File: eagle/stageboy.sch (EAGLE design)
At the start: 35 parts, among them IC1 MEGA8-P, IC2 7805TV, J1 POWER_JACKPTH, Q1 16MHz, X1 MIDI IN, X2 MIDI OUT, X4 22-23-2021, X6 GBIO

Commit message: Picked a board layout and named it accordingly
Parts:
- renumbered JP2 to GB5V
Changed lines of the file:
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@@
 <part name="C3" library="rcl" deviceset="C-US" device="025-025X050" value="22pF"/>
 <part name="C4" library="rcl" deviceset="C-US" device="025-025X050" value="22pF"/>
-<part name="JP2" library="jumper" deviceset="JP1Q" device="" value="GB5V"/>
+<part name="GB5V" library="jumper" deviceset="JP1Q" device="" value="GB5V"/>
 <part name="SUPPLY20" library="supply2" deviceset="+5V" device=""/>
 <part name="SUPPLY22" library="supply2" deviceset="+5V" device=""/>
@@
 <instance part="C3" gate="G$1" x="33.02" y="68.58" rot="R90"/>
 <instance part="C4" gate="G$1" x="33.02" y="53.34" rot="R90"/>
-<instance part="JP2" gate="A" x="157.48" y="116.84" rot="R180"/>
+<instance part="GB5V" gate="A" x="157.48" y="116.84" rot="R180"/>
 <instance part="SUPPLY20" gate="+5V" x="157.48" y="127"/>
 <instance part="SUPPLY22" gate="+5V" x="101.6" y="124.46" rot="R270"/>
@@
 <segment>
 <pinref part="SUPPLY20" gate="+5V" pin="+5V"/>
-<pinref part="JP2" gate="A" pin="1"/>
+<pinref part="GB5V" gate="A" pin="1"/>
 </segment>
 <segment>
@@
 <segment>
 <pinref part="X6" gate="G$1" pin="4"/>
-<pinref part="JP2" gate="A" pin="2"/>
+<pinref part="GB5V" gate="A" pin="2"/>
 <wire x1="157.48" y1="99.06" x2="157.48" y2="109.22" width="0.1524" layer="91"/>
 </segment>

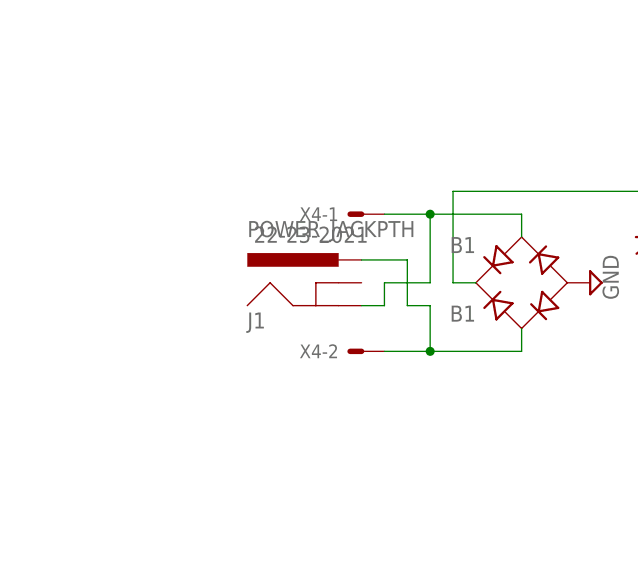
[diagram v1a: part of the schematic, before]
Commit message: Resized the electrolytic capacitors
The 2200uF cap was way too small, with the 22uF being only slightly
so. Both were changed and components shifted around as needed.
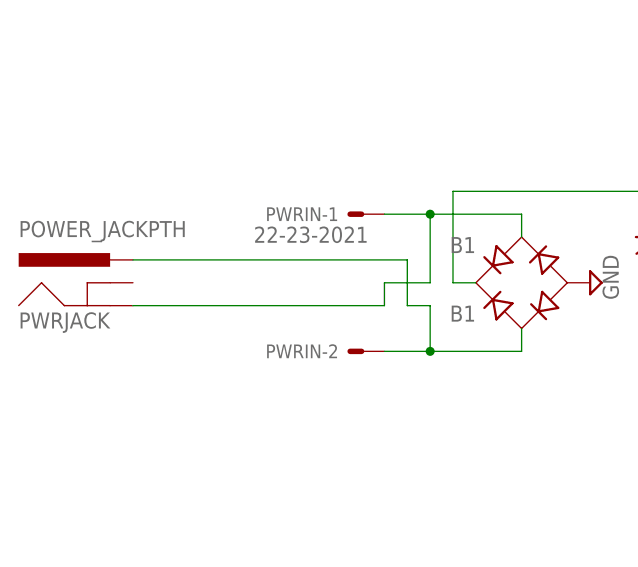
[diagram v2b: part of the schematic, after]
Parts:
- removed J1: POWER_JACKPTH, SparkFun-Connectors:POWER_JACKPTH
- added PWRJACK: POWER_JACKPTH, SparkFun-Connectors:POWER_JACKPTH
- C6: device resistor:CPOL-USE2.5-6 -> resistor:CPOL-USE2.5-7
- C7: device resistor:CPOL-USE3.5-10 -> resistor:CPOL-USE5-13
- renumbered X4 to PWRIN
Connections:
- net N$38: now also PWRJACK.GND; no longer J1.GND
- net N$39: now also PWRJACK.PWR; no longer J1.PWR
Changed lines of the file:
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@@
 <grid distance="0.1" unitdist="inch" unit="inch" style="lines" multiple="1" display="no" altdistance="0.01" altunitdist="inch" altunit="inch"/>
 <layers>
-<layer number="1" name="Top" color="4" fill="1" visible="no" active="no"/>
-<layer number="2" name="Route2" color="1" fill="3" visible="no" active="no"/>
-<layer number="3" name="Route3" color="4" fill="3" visible="no" active="no"/>
-<layer number="14" name="Route14" color="1" fill="6" visible="no" active="no"/>
-<layer number="15" name="Route15" color="4" fill="6" visible="no" active="no"/>
-<layer number="16" name="Bottom" color="1" fill="1" visible="no" active="no"/>
-<layer number="17" name="Pads" color="2" fill="1" visible="no" active="no"/>
-<layer number="18" name="Vias" color="2" fill="1" visible="no" active="no"/>
-<layer number="19" name="Unrouted" color="6" fill="1" visible="no" active="no"/>
-<layer number="20" name="Dimension" color="15" fill="1" visible="no" active="no"/>
-<layer number="21" name="tPlace" color="7" fill="1" visible="no" active="no"/>
-<layer number="22" name="bPlace" color="7" fill="1" visible="no" active="no"/>
-<layer number="23" name="tOrigins" color="15" fill="1" visible="no" active="no"/>
-<layer number="24" name="bOrigins" color="15" fill="1" visible="no" active="no"/>
-<layer number="25" name="tNames" color="7" fill="1" visible="no" active="no"/>
-<layer number="26" name="bNames" color="7" fill="1" visible="no" active="no"/>
-<layer number="27" name="tValues" color="7" fill="1" visible="no" active="no"/>
-<layer number="28" name="bValues" color="7" fill="1" visible="no" active="no"/>
+<layer number="1" name="Top" color="4" fill="1" visible="yes" active="no"/>
+<layer number="2" name="Route2" color="1" fill="3" visible="yes" active="no"/>
+<layer number="3" name="Route3" color="4" fill="3" visible="yes" active="no"/>
+<layer number="14" name="Route14" color="1" fill="6" visible="yes" active="no"/>
+<layer number="15" name="Route15" color="4" fill="6" visible="yes" active="no"/>
+<layer number="16" name="Bottom" color="1" fill="1" visible="yes" active="no"/>
+<layer number="17" name="Pads" color="2" fill="1" visible="yes" active="no"/>
+<layer number="18" name="Vias" color="2" fill="1" visible="yes" active="no"/>
+<layer number="19" name="Unrouted" color="6" fill="1" visible="yes" active="no"/>
+<layer number="20" name="Dimension" color="15" fill="1" visible="yes" active="no"/>
+<layer number="21" name="tPlace" color="7" fill="1" visible="yes" active="no"/>
+<layer number="22" name="bPlace" color="7" fill="1" visible="yes" active="no"/>
+<layer number="23" name="tOrigins" color="15" fill="1" visible="yes" active="no"/>
+<layer number="24" name="bOrigins" color="15" fill="1" visible="yes" active="no"/>
+<layer number="25" name="tNames" color="7" fill="1" visible="yes" active="no"/>
+<layer number="26" name="bNames" color="7" fill="1" visible="yes" active="no"/>
+<layer number="27" name="tValues" color="7" fill="1" visible="yes" active="no"/>
+<layer number="28" name="bValues" color="7" fill="1" visible="yes" active="no"/>
 <layer number="29" name="tStop" color="7" fill="3" visible="no" active="no"/>
 <layer number="30" name="bStop" color="7" fill="6" visible="no" active="no"/>
@@
 <layer number="35" name="tGlue" color="7" fill="4" visible="no" active="no"/>
 <layer number="36" name="bGlue" color="7" fill="5" visible="no" active="no"/>
-<layer number="37" name="tTest" color="7" fill="1" visible="no" active="no"/>
-<layer number="38" name="bTest" color="7" fill="1" visible="no" active="no"/>
+<layer number="37" name="tTest" color="7" fill="1" visible="yes" active="no"/>
+<layer number="38" name="bTest" color="7" fill="1" visible="yes" active="no"/>
 <layer number="39" name="tKeepout" color="4" fill="11" visible="no" active="no"/>
 <layer number="40" name="bKeepout" color="1" fill="11" visible="no" active="no"/>
@@
 <layer number="44" name="Drills" color="7" fill="1" visible="no" active="no"/>
 <layer number="45" name="Holes" color="7" fill="1" visible="no" active="no"/>
-<layer number="46" name="Milling" color="3" fill="1" visible="no" active="no"/>
-<layer number="47" name="Measures" color="7" fill="1" visible="no" active="no"/>
-<layer number="48" name="Document" color="7" fill="1" visible="no" active="no"/>
-<layer number="49" name="Reference" color="7" fill="1" visible="no" active="no"/>
-<layer number="50" name="dxf" color="7" fill="1" visible="no" active="no"/>
-<layer number="51" name="tDocu" color="7" fill="1" visible="no" active="no"/>
-<layer number="52" name="bDocu" color="7" fill="1" visible="no" active="no"/>
-<layer number="53" name="tGND_GNDA" color="7" fill="9" visible="no" active="no"/>
-<layer number="54" name="bGND_GNDA" color="1" fill="9" visible="no" active="no"/>
-<layer number="56" name="wert" color="7" fill="1" visible="no" active="no"/>
+<layer number="46" name="Milling" color="3" fill="1" visible="yes" active="no"/>
+<layer number="47" name="Measures" color="7" fill="1" visible="yes" active="no"/>
+<layer number="48" name="Document" color="7" fill="1" visible="yes" active="no"/>
+<layer number="49" name="Reference" color="7" fill="1" visible="yes" active="no"/>
+<layer number="50" name="dxf" color="7" fill="1" visible="yes" active="no"/>
+<layer number="51" name="tDocu" color="7" fill="1" visible="yes" active="no"/>
+<layer number="52" name="bDocu" color="7" fill="1" visible="yes" active="no"/>
+<layer number="53" name="tGND_GNDA" color="7" fill="9" visible="yes" active="no"/>
+<layer number="54" name="bGND_GNDA" color="1" fill="9" visible="yes" active="no"/>
+<layer number="56" name="wert" color="7" fill="1" visible="yes" active="no"/>
 <layer number="91" name="Nets" color="2" fill="1" visible="yes" active="yes"/>
 <layer number="92" name="Busses" color="1" fill="1" visible="yes" active="yes"/>
@@
 <part name="X2" library="con-hirschmann" deviceset="MAB5SH" device="" value="MIDI OUT"/>
 <part name="MIDI-IN" library="pinhead" deviceset="PINHD-1X2" device="" value="MIDI IN"/>
-<part name="C6" library="resistor" deviceset="CPOL-US" device="E2.5-6" value="22uF"/>
+<part name="C6" library="resistor" deviceset="CPOL-US" device="E2.5-7" value="22uF"/>
 <part name="SUPPLY16" library="supply2" deviceset="GND" device=""/>
-<part name="X4" library="con-molex" deviceset="22-23-2021" device=""/>
+<part name="PWRIN" library="con-molex" deviceset="22-23-2021" device=""/>
 <part name="IC2" library="linear" deviceset="78*" device="TV" technology="05"/>
 <part name="C5" library="rcl" deviceset="C-US" device="025-025X050" value="100nF"/>
@@
 <part name="SUPPLY7" library="supply2" deviceset="GND" device=""/>
 <part name="B1" library="rectifier" deviceset="RB1A" device="" value="B1"/>
-<part name="C7" library="resistor" deviceset="CPOL-US" device="E3.5-10" value="2200uF"/>
+<part name="C7" library="resistor" deviceset="CPOL-US" device="E5-13" value="2200uF"/>
 <part name="C8" library="rcl" deviceset="C-US" device="025-025X050" value="330nF"/>
 <part name="SUPPLY9" library="supply2" deviceset="GND" device=""/>
@@
 <part name="SUPPLY29" library="supply2" deviceset="GND" device=""/>
 <part name="5VDC" library="con-molex" deviceset="22-23-2021" device="" value="DCPWR"/>
-<part name="J1" library="SparkFun-Connectors" deviceset="POWER_JACK" device="PTH"/>
+<part name="PWRJACK" library="SparkFun-Connectors" deviceset="POWER_JACK" device="PTH"/>
 <part name="SUPPLY10" library="supply2" deviceset="GND" device=""/>
 </parts>
@@
 <instance part="C6" gate="G$1" x="86.36" y="119.38"/>
 <instance part="SUPPLY16" gate="GND" x="86.36" y="111.76"/>
-<instance part="X4" gate="-1" x="-10.16" y="121.92" rot="R180"/>
-<instance part="X4" gate="-2" x="-10.16" y="106.68" rot="R180"/>
+<instance part="PWRIN" gate="-1" x="-10.16" y="121.92" rot="R180"/>
+<instance part="PWRIN" gate="-2" x="-10.16" y="106.68" rot="R180"/>
 <instance part="IC2" gate="A1" x="48.26" y="124.46"/>
 <instance part="C5" gate="G$1" x="73.66" y="119.38"/>
@@
 <instance part="5VDC" gate="-1" x="101.6" y="139.7"/>
 <instance part="5VDC" gate="-2" x="101.6" y="137.16"/>
-<instance part="J1" gate="G$1" x="-12.7" y="109.22"/>
+<instance part="PWRJACK" gate="G$1" x="-38.1" y="109.22"/>
 <instance part="SUPPLY10" gate="GND" x="203.2" y="35.56" rot="R90"/>
 </instances>
@@
 <wire x1="7.62" y1="121.92" x2="-2.54" y2="121.92" width="0.1524" layer="91"/>
 <wire x1="-2.54" y1="121.92" x2="-2.54" y2="114.3" width="0.1524" layer="91"/>
-<pinref part="X4" gate="-1" pin="S"/>
+<pinref part="PWRIN" gate="-1" pin="S"/>
 <wire x1="-7.62" y1="121.92" x2="-2.54" y2="121.92" width="0.1524" layer="91"/>
 <junction x="-2.54" y="121.92"/>
 <wire x1="-2.54" y1="114.3" x2="-7.62" y2="114.3" width="0.1524" layer="91"/>
 <wire x1="-7.62" y1="114.3" x2="-7.62" y2="111.76" width="0.1524" layer="91"/>
-<wire x1="-7.62" y1="111.76" x2="-10.16" y2="111.76" width="0.1524" layer="91"/>
-<pinref part="J1" gate="G$1" pin="GND"/>
+<wire x1="-7.62" y1="111.76" x2="-35.56" y2="111.76" width="0.1524" layer="91"/>
+<pinref part="PWRJACK" gate="G$1" pin="GND"/>
 </segment>
 </net>
@@
 <wire x1="-2.54" y1="106.68" x2="7.62" y2="106.68" width="0.1524" layer="91"/>
 <wire x1="7.62" y1="106.68" x2="7.62" y2="109.22" width="0.1524" layer="91"/>
-<pinref part="X4" gate="-2" pin="S"/>
+<pinref part="PWRIN" gate="-2" pin="S"/>
 <wire x1="-7.62" y1="106.68" x2="-2.54" y2="106.68" width="0.1524" layer="91"/>
 <junction x="-2.54" y="106.68"/>
-<wire x1="-10.16" y1="116.84" x2="-5.08" y2="116.84" width="0.1524" layer="91"/>
+<wire x1="-35.56" y1="116.84" x2="-5.08" y2="116.84" width="0.1524" layer="91"/>
 <wire x1="-5.08" y1="116.84" x2="-5.08" y2="111.76" width="0.1524" layer="91"/>
 <wire x1="-5.08" y1="111.76" x2="-2.54" y2="111.76" width="0.1524" layer="91"/>
-<pinref part="J1" gate="G$1" pin="PWR"/>
-</segment>
-</net>
+<pinref part="PWRJACK" gate="G$1" pin="PWR"/>
+</segment>
+</net>

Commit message: Added Bill of Materials
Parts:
- C6: device resistor:CPOL-USE2.5-7 -> resistor:CPOL-USE2.5-5
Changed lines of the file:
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@@
 <part name="X2" library="con-hirschmann" deviceset="MAB5SH" device="" value="MIDI OUT"/>
 <part name="MIDI-IN" library="pinhead" deviceset="PINHD-1X2" device="" value="MIDI IN"/>
-<part name="C6" library="resistor" deviceset="CPOL-US" device="E2.5-7" value="22uF"/>
+<part name="C6" library="resistor" deviceset="CPOL-US" device="E2.5-5" value="22uF"/>
 <part name="SUPPLY16" library="supply2" deviceset="GND" device=""/>
 <part name="PWRIN" library="con-molex" deviceset="22-23-2021" device=""/>
